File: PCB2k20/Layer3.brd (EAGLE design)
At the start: 180 x 187.8 mm, 42 parts

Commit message: Layer 3 placement kinda done, routing to wait for layer 1 signals to be confirmed. also renamed some folders because windows explorer doesnt like the old name
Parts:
- removed 1C11: 1uF, JH:C0603
- removed 1C7, 1C8: 20pF, JH:C0603
- removed 1R5: 1k, JH:R0603
- removed 1S2: MOMENTARY_SWITCH_4X3, JH:MOMENTARY_SWITCH_4X3
- removed R3: 10k, JH:R0603
- added 1C2: 1uF, JH:C0603
- added 1C5, 1C6: 20pF, JH:C0603
- added 1R2: 10k, JH:R0603
- added 1R3: 1k, JH:R0603
- added 1SW1: MOMENTARY_SWITCH_4X3, JH:MOMENTARY_SWITCH_4X3
- SWD: value (none) -> JST_04-V; device SparkFun-Connectors:1X04_LOCK -> JH:JST_04-V
- moved S1 284.5 mm to (57.8, -14.0), turned to 90 degrees
- moved R1 275.9 mm to (-9.53, 62.2), turned to 90 degrees
- moved R2 275.4 mm to (-9.53, 58.4), turned to 270 degrees
- moved 1C4 184.9 mm to (-29.8, -14.6)
- moved 1C3 183.5 mm to (-33.9, -27.3), turned to 180 degrees
- moved 1U1 179.1 mm to (-34.9, -19.7)
- moved 2C1 177.2 mm to (-26.0, 42.5), turned to 270 degrees
- moved 2R2 173.4 mm to (-32.4, 38.7), turned to 180 degrees
- moved 2C2 172.6 mm to (-22.2, 42.5), turned to 270 degrees
- moved 2C3 170.6 mm to (-34.3, 48.3), turned to 90 degrees
- moved 2D1 163.5 mm to (-29.2, 48.3)
- moved 2C4 158.6 mm to (-34.9, 34.9), turned to 180 degrees
- moved 1C1 154.4 mm to (-38.7, -12.7)
- moved 2L1 154.2 mm to (-40.6, 46.4), turned to 270 degrees
- moved 2R1 154.1 mm to (-36.8, 38.7), turned to 180 degrees
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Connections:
- net 3.3V: now also 1C2.1, 1R2.2; no longer 1C11.1, 1R4.2
- net GND: now also 1C2.2, 1C5.2, 1C6.2, 1R3.1, 1R4.2; no longer 1C11.2, 1C7.2, 1C8.2, 1R5.1, R3.2
- net N$23: now also 1R4.1; no longer R3.1
- net N$4: now also 1R3.2, 1SW1.P$1; no longer 1R5.2, 1S2.P$1
- net OSC_IN: now also 1C5.1; no longer 1C7.1
- net OSC_OUT: now also 1C6.1; no longer 1C8.1
- net RESET: now also 1R2.1, 1SW1.P$2; no longer 1R4.1, 1S2.P$2
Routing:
- net 5V: track 0.00 -> 99.3 mm
- net SWDIO: track 0.00 -> 34.6 mm
- net SWDCLK: track 0.00 -> 33.0 mm
- net 3.3V: track 0.00 -> 30.7 mm, vias 0 -> 2
- net OSC_IN: track 0.00 -> 16.4 mm
- net IMU_SDA: track 0.00 -> 12.2 mm
- net OSC_OUT: track 0.00 -> 11.9 mm
- net IMU_SCL: track 0.00 -> 11.1 mm
- net N$7: track 0.00 -> 5.84 mm
- net BT_KEY: track 0.00 -> 5.26 mm
- net RESET: track 0.00 -> 3.37 mm
- net N$4: track 0.00 -> 3.37 mm
- net N$3: track 0.00 -> 3.19 mm
- net N$8: track 0.00 -> 2.36 mm
- net BATT_LVL: track 0.00 -> 2.11 mm
- added copper zone on layer 1, net 5V
- added copper zone on layer 1, net N$6

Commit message: continue on layer 1 schematic, just need to finish this asap and quickly start positioning
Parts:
- added U$2: XT60XT60PW-F, JH:XT60PW-F
- 2R2: value 5.9k -> 3.24k
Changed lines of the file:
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@@
 <drawing>
 <settings>
-<setting alwaysvectorfont="no"/>
+<setting alwaysvectorfont="yes"/>
 <setting verticaltext="up"/>
 </settings>
@@
 </layers>
 <board>
-<fusionsync huburn="a.cGVyc29uYWw6dWUyYTI4NGEw" projecturn="a.cGVyc29uYWw6dWUyZDRiOTQ5IzIwMjAwMTEzMjU0NTYzOTU2" f3durn="urn:adsk.wipprod:dm.lineage:Xl7cFy5cSp2rGe9-XsMr_g" pcbguid="373dfac2-5937-4cc6-8f6c-6a4faf37fafa" lastpulledtime="" lastsyncedchangeguid="095beb08-3190-7c29-25b8-67f11cd41706"/>
+<fusionsync huburn="a.cGVyc29uYWw6dWUyYTI4NGEw" projecturn="a.cGVyc29uYWw6dWUyZDRiOTQ5IzIwMjAwMTEzMjU0NTYzOTU2" f3durn="urn:adsk.wipprod:dm.lineage:Xl7cFy5cSp2rGe9-XsMr_g" pcbguid="373dfac2-5937-4cc6-8f6c-6a4faf37fafa" lastpulledtime="" lastsyncedchangeguid="8b7e9732-4c04-7fd7-da55-9236ac645420"/>
 <plain>
 <hole x="-24.549" y="-23.836" drill="3"/>
@@
 <attribute name="VALUE" x="-34.925" y="30.353" size="0.7112" layer="27" font="vector" ratio="18" align="top-center"/>
 </element>
-<element name="2R2" library="JH" library_urn="urn:adsk.eagle:library:6027132" package="R0603" package3d_urn="urn:adsk.eagle:package:15441228/3" value="5.9k" x="-32.385" y="38.735" smashed="yes" rot="R180">
+<element name="2R2" library="JH" library_urn="urn:adsk.eagle:library:6027132" package="R0603" package3d_urn="urn:adsk.eagle:package:15441228/3" value="3.24k" x="-32.385" y="38.735" smashed="yes" rot="R180">
 <attribute name="NAME" x="-32.385" y="37.973" size="0.7112" layer="25" font="vector" ratio="18" rot="R180" align="bottom-center"/>
 <attribute name="VALUE" x="-32.385" y="39.497" size="0.7112" layer="27" font="vector" ratio="18" rot="R180" align="top-center"/>
@@
 </element>
 <element name="PCB1" library="JH" library_urn="urn:adsk.eagle:library:6027132" package="RPI3" package3d_urn="urn:adsk.eagle:package:9592022/2" value="RPI3" x="-28" y="37.655" smashed="yes" rot="R270"/>
+<element name="U$2" library="JH" library_urn="urn:adsk.eagle:library:6027132" package="XT60PW-F" package3d_urn="urn:adsk.eagle:package:16411181/4" value="XT60XT60PW-F" x="2.54" y="-58.42" smashed="yes">
+<attribute name="NAME" x="-5.08" y="-55.88" size="1.27" layer="25"/>
+</element>
 </elements>
 <signals>

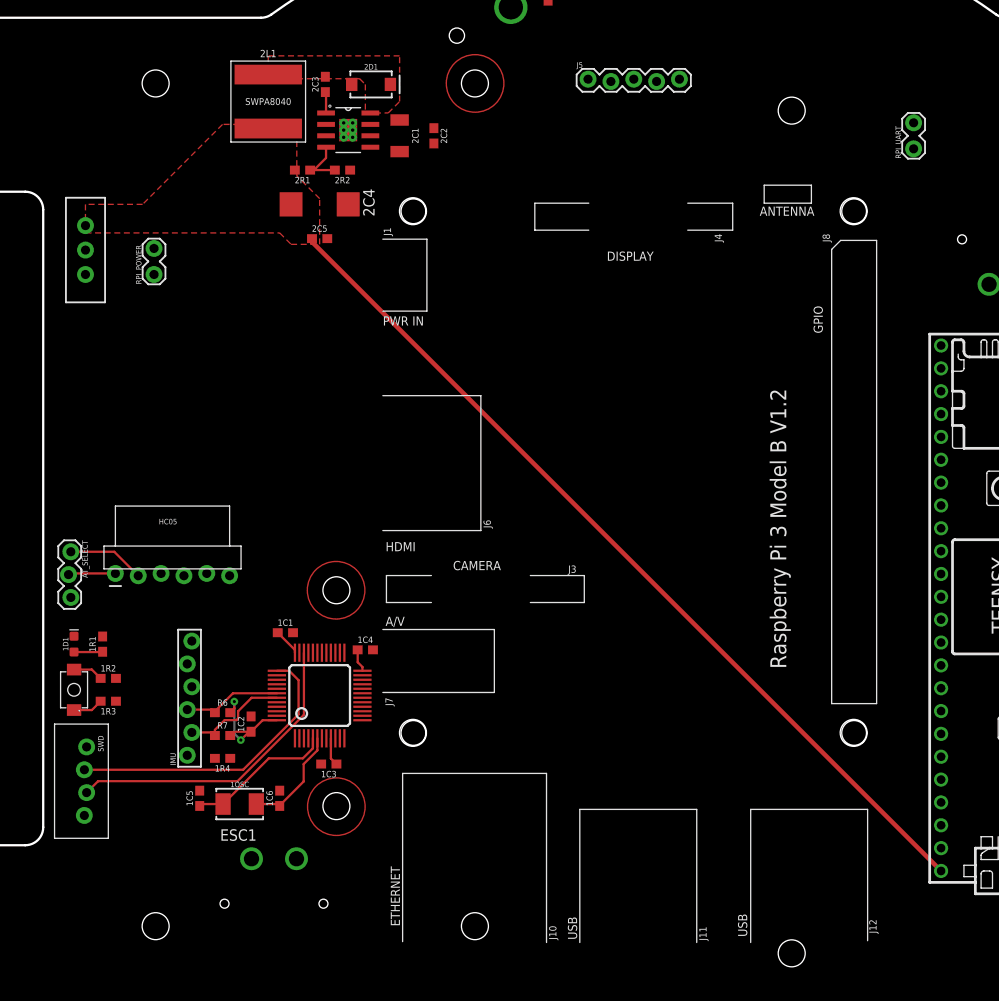
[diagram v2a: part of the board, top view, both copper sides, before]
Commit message: added a switch to choose between programmer power and battery power for STM32
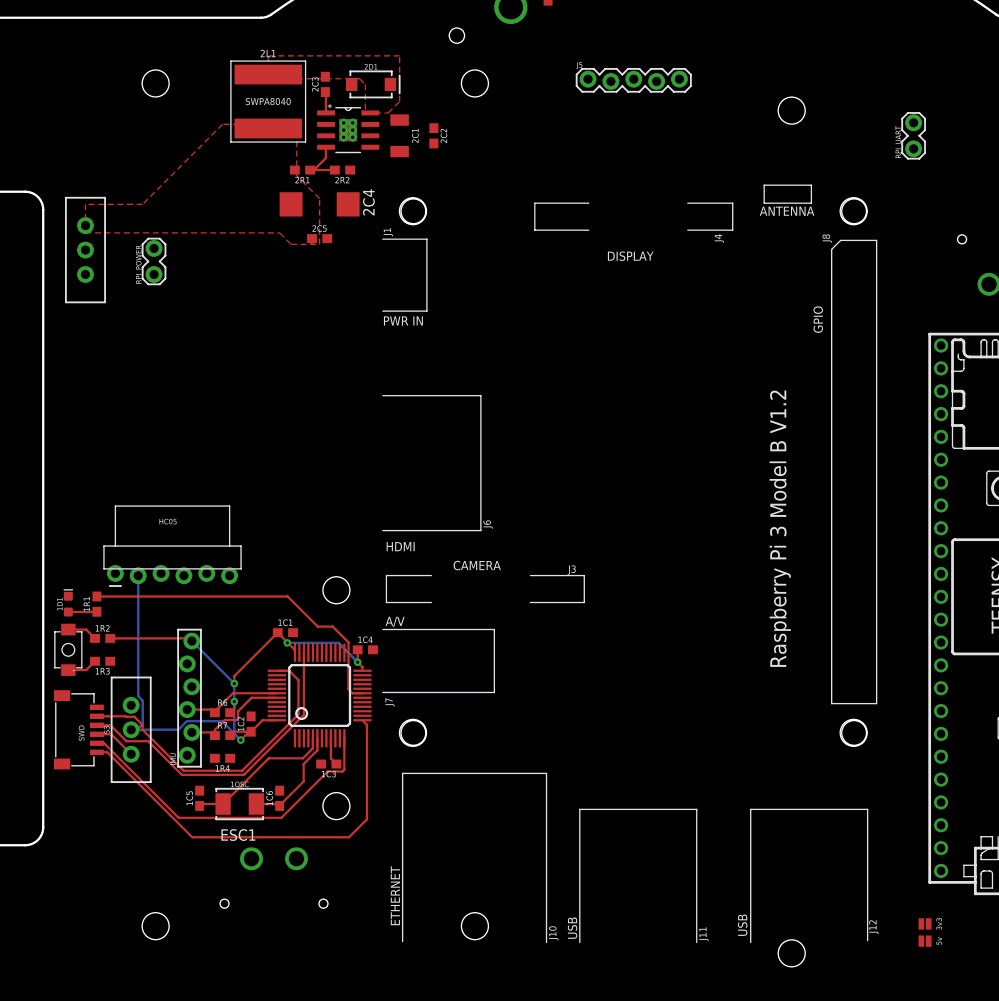
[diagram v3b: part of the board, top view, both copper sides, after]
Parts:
- removed AT_SELECT: CONN_03, JH:1X03_LOCK
- added JP1, JP2: JUMPER-SMT_2_NO_NO-SILK, SparkFun-Jumpers:SMT-JUMPER_2_NO_NO-SILK
- added S3: (no value), SparkFun-Switches:SWITCH_SPDT_PTH_11.6X4.0MM_LOCK
- SWD: value JST_04-V -> SM06B-SRSS-TB; device JH:JST_04-V -> con-JST SH:SM06B-SRSS-TB
- moved 1D1 4.49 mm to (-62.9, -9.53)
- moved 1SW1 4.49 mm to (-62.9, -14.6)
- moved 1R1 4.49 mm to (-59.7, -9.53)
- moved 1R2 4.49 mm to (-59.1, -13.3)
- moved 1R3 4.49 mm to (-59.1, -15.9)
- moved SWD 2.29 mm to (-59.7, -23.5), turned to 90 degrees
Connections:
- removed net BT_KEY: AT_SELECT.2, HC05.1
- removed net BT_STATE: HC05.6
- new net 3.3V_MCU: 1C1.1, 1C2.1, 1C3.1, 1C4.1, 1R2.2, 1U1.24, 1U1.36, 1U1.48, 1U1.9, HC05.2, IMU.6, R6.2, R7.2, S3.2
- new net 3.3V_PROG: S3.3, SWD.4
- new net DEBUG_RX: 1U1.13, SWD.6
- new net DEBUG_TX: 1U1.12, SWD.5
- new net N$1: JP1.1, U$1.VIN
- new net N$2: JP2.1, U$1.3V3_LO
- net 3.3V: now also JP2.2, S3.1; no longer 1C1.1, 1C2.1, 1C3.1, 1C4.1, 1R2.2, 1U1.24, 1U1.36, 1U1.48, 1U1.9, AT_SELECT.1, HC05.2, IMU.6, R6.2, R7.2, SWD.4
- net 5V: now also JP1.2; no longer U$1.VIN
- net GND: no longer AT_SELECT.3
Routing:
- net 5V: track 99.3 -> 0.36 mm
- net 3.3V_MCU: track 0.00 -> 86.2 mm, vias 0 -> 5
- net DEBUG_RX: track 0.00 -> 46.0 mm
- net 33: track 0.00 -> 37.0 mm
- net DEBUG_TX: track 0.00 -> 36.7 mm
- net 3.3V: track 30.7 -> 0.00 mm, vias 2 -> 0
- net BT_KEY: track 5.26 -> 0.00 mm
- net 3.3V_PROG: track 0.00 -> 4.73 mm
- net SWDCLK: track 33.0 -> 34.5 mm
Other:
- board text added: "3v3"
- board text added: "5v"

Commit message: done just need to silkscreen now!!!
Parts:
- added J1, J3, J4, J6: 14AWG, JH:14AWG
- added J2: CONN_03, JH:1X03_LOCK
- added R10, R3, R4, R5, R8, R9: (no value), JH:R0603
- added X1: BM10B-SRSS-TB, con-JST SH:BM10B-SRSS-TB
- RPI_UART: device SparkFun-Connectors:1X02_LOCK -> SparkFun-Connectors:1X06_LOCK
- S1: value DIP-04SMD -> DIP-06; device SparkFun-Switches:DIPSWITCH-04-SMD -> SparkFun-Switches:DIPSWITCH-06-SMD
- moved RPI_UART 38.9 mm to (55.2, 10.8)
- moved S1 14.0 mm to (57.8, 0.00)
- moved J5 3.81 mm to (-5.08, 52.5)
- moved JP1 1.91 mm to (32.4, -45.1), turned to 180 degrees
- moved JP2 1.91 mm to (32.4, -47.0), turned to 180 degrees
- moved 1C3 0.54 mm to (-34.3, -27.7)
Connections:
- new net INM1: U$1.A21/DAC0, X1.8
- new net INM2: U$1.A22/DAC1, X1.6
- new net INM3: U$1.13/SCK, X1.4
- new net INM4: U$1.14/A0, X1.2
- new net L1_RX: U$1.33/A14, X1.9
- new net L1_TX: U$1.34/A15, X1.10
- new net LIGHT_INT: J2.1, U$1.39/A20
- new net N$10: R3.1, S1.12, U$1.24
- new net N$11: R5.1, S1.10, U$1.26
- new net N$12: R8.1, S1.9, U$1.27
- new net N$5: R4.1, S1.11, U$1.25
- new net PWMM1: U$1.35/A16, X1.7
- new net PWMM2: U$1.36/A17, X1.5
- new net PWMM3: U$1.37/A18, X1.3
- new net PWMM4: U$1.38/A19, X1.1
- new net RPI_1: R10.1, RPI_UART.2, S1.7
- new net RPI_2: R9.1, RPI_UART.1, S1.8
- net 12V: now also J1.P$1, J3.P$1, U$2.+
- net 3.3V: now also J2.3, R10.2, R3.2, R4.2, R5.2, R8.2, R9.2
- net BATT_LVL: now also U$1.15/A1
- net BT_RX: now also U$1.8
- net BT_TX: now also U$1.7
- net GND: now also J2.2, J4.P$1, J6.P$1, S1.1, S1.2, S1.3, S1.4, S1.5, S1.6, U$2.-
- net L3_RX: now also U$1.1/TX
- net L3_TX: now also U$1.0/RX
- net L4_RX: now also U$1.10/CS
- net L4_TX: now also U$1.9/CS
- net RPI_RX: now also RPI_UART.5, U$1.32/A13; no longer RPI_UART.1, U$1.0/RX
- net RPI_TX: now also RPI_UART.6, U$1.31/A12; no longer RPI_UART.2, U$1.1/TX
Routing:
- net 3.3V: track 0.00 -> 311.3 mm, vias 0 -> 4
- net 12V: track 0.00 -> 264.6 mm, vias 0 -> 1
- net 5V: track 0.36 -> 196.2 mm, vias 0 -> 4
- net BT_TX: track 0.00 -> 104.6 mm
- net BT_RX: track 0.00 -> 101.7 mm
- net L4_RX: track 0.00 -> 100.5 mm, vias 0 -> 1
- net L4_TX: track 0.00 -> 100.0 mm
- net L3_RX: track 0.00 -> 97.0 mm, vias 0 -> 1
- net BATT_LVL: track 2.11 -> 98.9 mm, vias 0 -> 2
- net L3_TX: track 0.00 -> 96.5 mm, vias 0 -> 1
- net RESET: track 3.37 -> 39.3 mm, vias 0 -> 2
- net L1_RX: track 0.00 -> 25.1 mm, vias 0 -> 2
- net PWMM1: track 0.00 -> 23.9 mm, vias 0 -> 2
- net PWMM2: track 0.00 -> 23.3 mm, vias 0 -> 2
- net L1_TX: track 0.00 -> 22.9 mm, vias 0 -> 2
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- added copper zone on layer 1, net 12V
- added copper zone on layer 1, net GND
- added copper zone on layer 16, net GND

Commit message: add gerbers, please everything turn out well!
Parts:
- added D1: BLUE, SparkFun-LED:LED-0603
- added R11: 1k, JH:R0603
- 2L1: value SWPA8040/10uH -> 10uH
- flipped J2 to the bottom
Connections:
- new net N$13: R11.2, RPI_UART.4
- new net N$14: D1.A, R11.1
- net GND: now also D1.C
- net IMU_RST: now also 1U1.2
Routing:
- net IMU_RST: track 0.00 -> 14.6 mm
- net 12V: track 264.6 -> 278.6 mm, vias 1 -> 7
- net N$14: track 0.00 -> 8.19 mm, vias 0 -> 2
- net N$13: track 0.00 -> 3.01 mm
- net GND: vias 21 -> 80
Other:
- board text added: "12v"
- board text added: "dip1"
- board text added: "dip2"
- board text added: "gnd"
- board text added: "led"
- board text added: "light int"
- board text added: "off"
- board text added: "on"
- board text added: "prog power"
- board text added: "rst"
- board text added: "rx"
- board text added: "scl"
- board text added: "sda"
- board text added: "tx"

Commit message: update values
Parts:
- R1: value 300k -> 30k
- R10, R3, R4, R5, R8, R9: value (none) -> 10k
- R2: value 100k -> 10k
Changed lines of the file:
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@@
 <drawing>
 <settings>
-<setting alwaysvectorfont="yes"/>
+<setting alwaysvectorfont="no"/>
 <setting verticaltext="up"/>
 </settings>
@@
 <attribute name="VALUE" x="-51.308" y="26.035" size="0.6096" layer="27" font="vector" ratio="20" rot="R90"/>
 </element>
-<element name="R1" library="JH" library_urn="urn:adsk.eagle:library:6027132" package="R0603" package3d_urn="urn:adsk.eagle:package:15441228/3" value="300k" x="-9.525" y="62.23" smashed="yes" rot="R90">
+<element name="R1" library="JH" library_urn="urn:adsk.eagle:library:6027132" package="R0603" package3d_urn="urn:adsk.eagle:package:15441228/3" value="30k" x="-9.525" y="62.23" smashed="yes" rot="R90">
 <attribute name="NAME" x="-10.287" y="62.23" size="0.7112" layer="25" font="vector" ratio="18" rot="R90" align="bottom-center"/>
 <attribute name="VALUE" x="-8.763" y="62.23" size="0.7112" layer="27" font="vector" ratio="18" rot="R90" align="top-center"/>
 </element>
-<element name="R2" library="JH" library_urn="urn:adsk.eagle:library:6027132" package="R0603" package3d_urn="urn:adsk.eagle:package:15441228/3" value="100k" x="-9.525" y="58.42" smashed="yes" rot="R270">
+<element name="R2" library="JH" library_urn="urn:adsk.eagle:library:6027132" package="R0603" package3d_urn="urn:adsk.eagle:package:15441228/3" value="10k" x="-9.525" y="58.42" smashed="yes" rot="R270">
 <attribute name="NAME" x="-10.287" y="58.42" size="0.7112" layer="25" font="vector" ratio="18" rot="R90" align="bottom-center"/>
 <attribute name="VALUE" x="-8.763" y="58.42" size="0.7112" layer="27" font="vector" ratio="18" rot="R90" align="top-center"/>
@@
 <element name="X1" library="con-JST SH" library_urn="urn:adsk.eagle:library:17006044" package="BM10B-SRSS-TB" package3d_urn="urn:adsk.eagle:package:17006089/1" override_package3d_urn="urn:adsk.eagle:package:17006089/2" override_package_urn="urn:adsk.eagle:footprint:17006088/1" value="BM10B-SRSS-TB" x="22.225" y="0" smashed="yes" rot="MR270"/>
 <element name="J2" library="JH" library_urn="urn:adsk.eagle:library:6027132" package="1X03_LOCK" package3d_urn="urn:adsk.eagle:package:15924798/2" value="CONN_03" x="23.495" y="9.525" smashed="yes" rot="MR90"/>
-<element name="R3" library="JH" library_urn="urn:adsk.eagle:library:6027132" package="R0603" package3d_urn="urn:adsk.eagle:package:15441228/3" value="" x="45.72" y="-0.635" smashed="yes" rot="R180">
+<element name="R3" library="JH" library_urn="urn:adsk.eagle:library:6027132" package="R0603" package3d_urn="urn:adsk.eagle:package:15441228/3" value="10k" x="45.72" y="-0.635" smashed="yes" rot="R180">
 <attribute name="NAME" x="45.72" y="-1.397" size="0.7112" layer="25" font="vector" ratio="18" rot="R180" align="bottom-center"/>
 <attribute name="VALUE" x="45.72" y="0.127" size="0.7112" layer="27" font="vector" ratio="18" rot="R180" align="top-center"/>
 </element>
-<element name="R4" library="JH" library_urn="urn:adsk.eagle:library:6027132" package="R0603" package3d_urn="urn:adsk.eagle:package:15441228/3" value="" x="45.72" y="2.54" smashed="yes" rot="R180">
+<element name="R4" library="JH" library_urn="urn:adsk.eagle:library:6027132" package="R0603" package3d_urn="urn:adsk.eagle:package:15441228/3" value="10k" x="45.72" y="2.54" smashed="yes" rot="R180">
 <attribute name="NAME" x="45.72" y="1.778" size="0.7112" layer="25" font="vector" ratio="18" rot="R180" align="bottom-center"/>
 <attribute name="VALUE" x="45.72" y="3.302" size="0.7112" layer="27" font="vector" ratio="18" rot="R180" align="top-center"/>
 </element>
-<element name="R5" library="JH" library_urn="urn:adsk.eagle:library:6027132" package="R0603" package3d_urn="urn:adsk.eagle:package:15441228/3" value="" x="45.72" y="5.715" smashed="yes" rot="R180">
+<element name="R5" library="JH" library_urn="urn:adsk.eagle:library:6027132" package="R0603" package3d_urn="urn:adsk.eagle:package:15441228/3" value="10k" x="45.72" y="5.715" smashed="yes" rot="R180">
 <attribute name="NAME" x="45.72" y="4.953" size="0.7112" layer="25" font="vector" ratio="18" rot="R180" align="bottom-center"/>
 <attribute name="VALUE" x="45.72" y="6.477" size="0.7112" layer="27" font="vector" ratio="18" rot="R180" align="top-center"/>
 </element>
-<element name="R8" library="JH" library_urn="urn:adsk.eagle:library:6027132" package="R0603" package3d_urn="urn:adsk.eagle:package:15441228/3" value="" x="45.72" y="8.89" smashed="yes" rot="R180">
+<element name="R8" library="JH" library_urn="urn:adsk.eagle:library:6027132" package="R0603" package3d_urn="urn:adsk.eagle:package:15441228/3" value="10k" x="45.72" y="8.89" smashed="yes" rot="R180">
 <attribute name="NAME" x="45.72" y="8.128" size="0.7112" layer="25" font="vector" ratio="18" rot="R180" align="bottom-center"/>
 <attribute name="VALUE" x="45.72" y="9.652" size="0.7112" layer="27" font="vector" ratio="18" rot="R180" align="top-center"/>
 </element>
-<element name="R9" library="JH" library_urn="urn:adsk.eagle:library:6027132" package="R0603" package3d_urn="urn:adsk.eagle:package:15441228/3" value="" x="59.055" y="10.795" smashed="yes">
+<element name="R9" library="JH" library_urn="urn:adsk.eagle:library:6027132" package="R0603" package3d_urn="urn:adsk.eagle:package:15441228/3" value="10k" x="59.055" y="10.795" smashed="yes">
 <attribute name="NAME" x="59.055" y="11.557" size="0.7112" layer="25" font="vector" ratio="18" align="bottom-center"/>
 <attribute name="VALUE" x="59.055" y="10.033" size="0.7112" layer="27" font="vector" ratio="18" align="top-center"/>
 </element>
-<element name="R10" library="JH" library_urn="urn:adsk.eagle:library:6027132" package="R0603" package3d_urn="urn:adsk.eagle:package:15441228/3" value="" x="59.055" y="13.335" smashed="yes">
+<element name="R10" library="JH" library_urn="urn:adsk.eagle:library:6027132" package="R0603" package3d_urn="urn:adsk.eagle:package:15441228/3" value="10k" x="59.055" y="13.335" smashed="yes">
 <attribute name="NAME" x="59.055" y="14.097" size="0.7112" layer="25" font="vector" ratio="18" align="bottom-center"/>
 <attribute name="VALUE" x="59.055" y="12.573" size="0.7112" layer="27" font="vector" ratio="18" align="top-center"/>

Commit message: BROKEN VERSION for 3d models
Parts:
- removed HC05: (no value), SparkFun-Connectors:MOLEX_1X6_RA_LOCK
- removed S2, S3: (no value), SparkFun-Switches:SWITCH_SPDT_PTH_11.6X4.0MM_LOCK
- added U$3, U$4: SWITCH_SPDT_TH, JH:SWITCH_SPDT_PTH_11.6X4.0MM_LOCK
- added U2: HC-05_BENT, JH:HC-05_BENT
- 1D1, D1: device SparkFun-LED:LED-0603 -> JH:LED-0603
- 1OSC: device SparkFun-Clocks:CRYSTAL-SMD-5X3.2-2PAD -> JH:CRYSTAL-SMD-5X3.2-2PAD
- 2D1: device SparkFun-DiscreteSemi:SMA-DIODE -> JH:SMA-DIODE
- J5: device SparkFun-Connectors:1X05_LOCK -> Connectors:1X05_LOCK
- RPI_POWER: device SparkFun-Connectors:1X02_LOCK -> Connectors:1X02_LOCK
- RPI_UART: device SparkFun-Connectors:1X06_LOCK -> Connectors:1X06_LOCK
- S1: device SparkFun-Switches:DIPSWITCH-06-SMD -> JH:DIPSWITCH-06-SMD
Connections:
- net 3.3V: now also U$3.1; no longer S3.1
- net 3.3V_MCU: now also U$3.2, U2.5; no longer HC05.2, S3.2
- net 3.3V_PROG: now also U$3.3; no longer S3.3
- net 5V: now also U$4.1; no longer S2.1
- net BT_RX: now also U2.2; no longer HC05.5
- net BT_TX: now also U2.3; no longer HC05.4
- net GND: now also U2.4; no longer HC05.3
- net N$9: now also U$4.2; no longer S2.2
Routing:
- net 3.3V_MCU: track 99.1 -> 85.7 mm
- net N$9: track 7.69 -> 0.25 mm
- net BT_TX: track 104.6 -> 97.4 mm
- net BT_RX: track 101.7 -> 95.0 mm
